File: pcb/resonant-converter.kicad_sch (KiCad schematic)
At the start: 30 parts, among them J1 Banana_Jack_Keystone_575-8, J2 Banana_Jack_Keystone_575-8, J3 Banana_Jack_Keystone_575-8, J4 Banana_Jack_Keystone_575-8, Q1 SIS472DN-T1-GE3, Q2 SIS472DN-T1-GE3, Q3 SIS472DN-T1-GE3, Q4 SIS472DN-T1-GE3, T1 B66206W1110T001, U1 UCC256610DDBR, U2 TEA2096T/1J, U4 PC817X2CSP9F, U5 TL431AIDBVR

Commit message: [#3] Add input capacitors and power indicator LED, change GND names on primary and secondary
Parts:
- added D3: LED-R-0603_KT-0603R, DW-footprints:LED_0603_1608Metric_R, symbol DW-diodes:LED-R-0603_KT-0603R
- added R10, R5: R-10k-0402, DW-footprints:R_0402_1005Metric, symbol DW-resistors:R-10k-0402
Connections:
- net GNDPWR is gone; now on net GND: C2.1, C3.1, C4.1, C5.1, C6.1, C7.1, J2.1, Q4.1 (S), Q4.2 (S), Q4.3 (S), U1.10 (GNDP)
- net GND: now also D3.1 (C); no longer D1.2 (A), D2.2 (A), Q1.1 (S), Q1.2 (S), Q1.3 (S), Q2.1 (S), Q2.2 (S), Q2.3 (S), R6.1, U2.2 (GND), U2.4 (SSB), U2.5 (SSA), U5.5 (A)
- net VCC: now also R10.2
- net at Q3.4 (G), U1.15 (HO): no longer C1.2
- net at L1.1, Q3.1 (S), Q3.2 (S)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: now also C1.2
- net GND_ISO: now reaches J4.1
- net GND_ISO: now also D1.2 (A), D2.2 (A), Q1.1 (S), Q1.2 (S), Q1.3 (S), Q2.1 (S), Q2.2 (S), Q2.3 (S), R6.1, U2.2 (GND), U2.4 (SSB), U2.5 (SSA), U5.5 (A)
- new net: D3.2 (A), R5.1
- new net: R10.1, R5.2

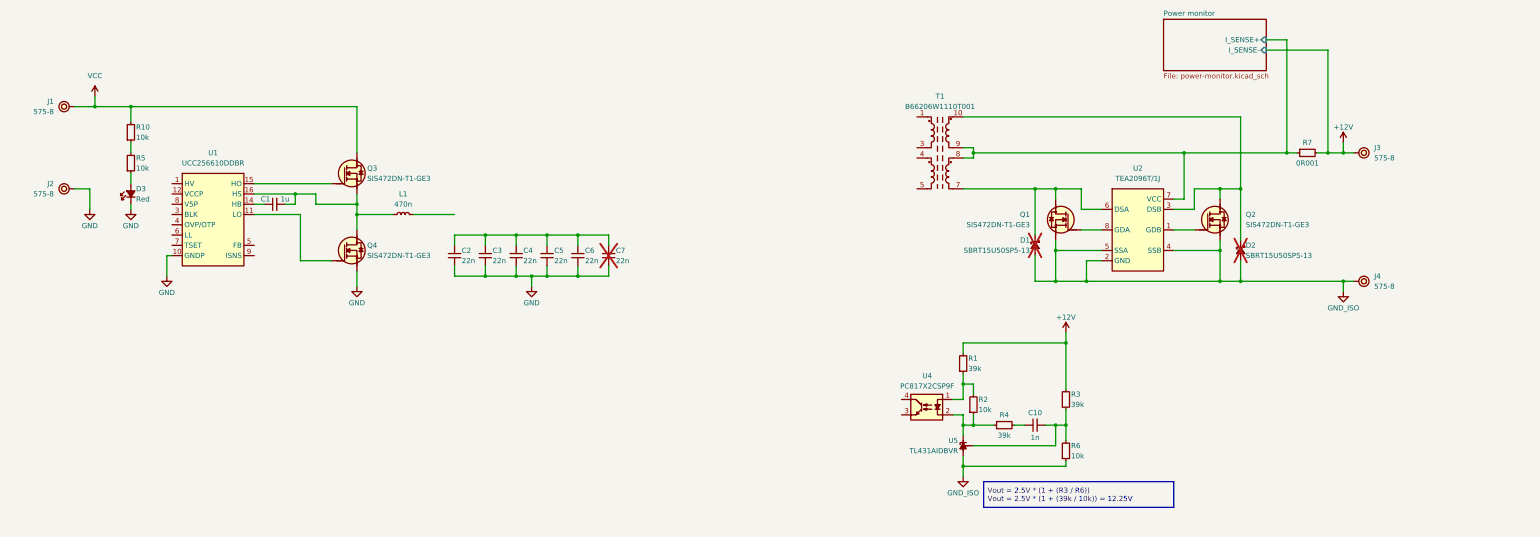
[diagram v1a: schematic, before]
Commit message: [#4] Sch: Add input and output capacitors, pri-sec interference capacitor and QWIIC connector, refactor schematic
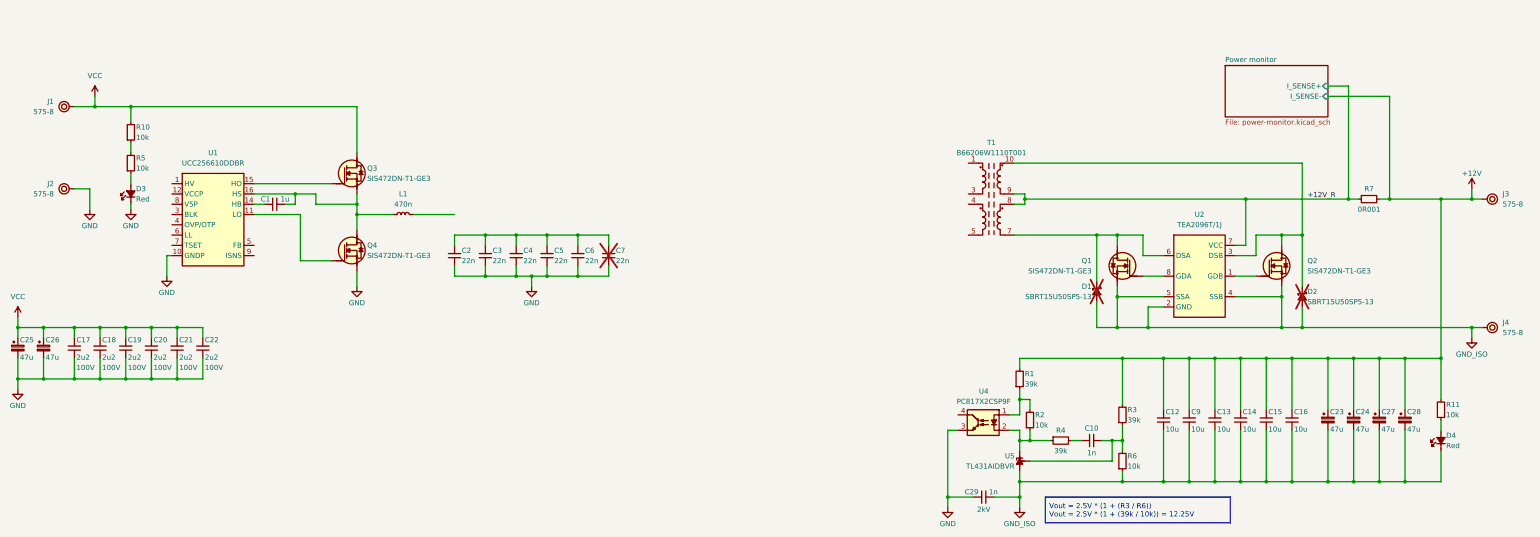
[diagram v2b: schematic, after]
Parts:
- added C12, C13, C14, C15, C16, C9: C-10u-0603, DW-footprints:C_0603_1608Metric, symbol DW-capacitors:C-10u-0603
- added C17, C18, C19, C20, C21, C22: C-2u2-100V-1206, DW-footprints:C_1206_3216Metric, symbol DW-capacitors:C-2u2-100V-1206
- added C23, C24, C25, C26, C27, C28: C_Pol_47u_100V_D8mm_H11.5, DW-footprints:C_Pol_D8mm_H11.5mm_P3.5mm, symbol DW-capacitors:C_Pol_47u_100V_D8mm_H11.5
- added C29: C-1n-2kV-1206, DW-footprints:C_1206_3216Metric, symbol DW-capacitors:C-1n-2kV-1206
- added D4: LED-R-0603_KT-0603R, DW-footprints:LED_0603_1608Metric_R, symbol DW-diodes:LED-R-0603_KT-0603R
- added R11: R-10k-0402, DW-footprints:R_0402_1005Metric, symbol DW-resistors:R-10k-0402
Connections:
- net +12V: now also C12.2, C13.2, C14.2, C15.2, C16.2, C23.1, C24.1, C27.1, C28.1, C9.2, R11.2
- net GND: now also U4.3, C17.1, C18.1, C19.1, C20.1, C21.1, C22.1, C25.2, C26.2, C29.1
- net GND_ISO: now also C12.1, C13.1, C14.1, C15.1, C16.1, C23.2, C24.2, C27.2, C28.2, C29.2, C9.1, D4.1 (C)
- net VCC: now also C17.2, C18.2, C19.2, C20.2, C21.2, C22.2, C25.1, C26.1
- net Power monitor/I_SENSE+ renamed +12V_R
- new net: D4.2 (A), R11.1
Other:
- moved on the sheet: C10, D1, D2, J3, J4, Q1, Q2, R1, R2, R3, R4, R6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

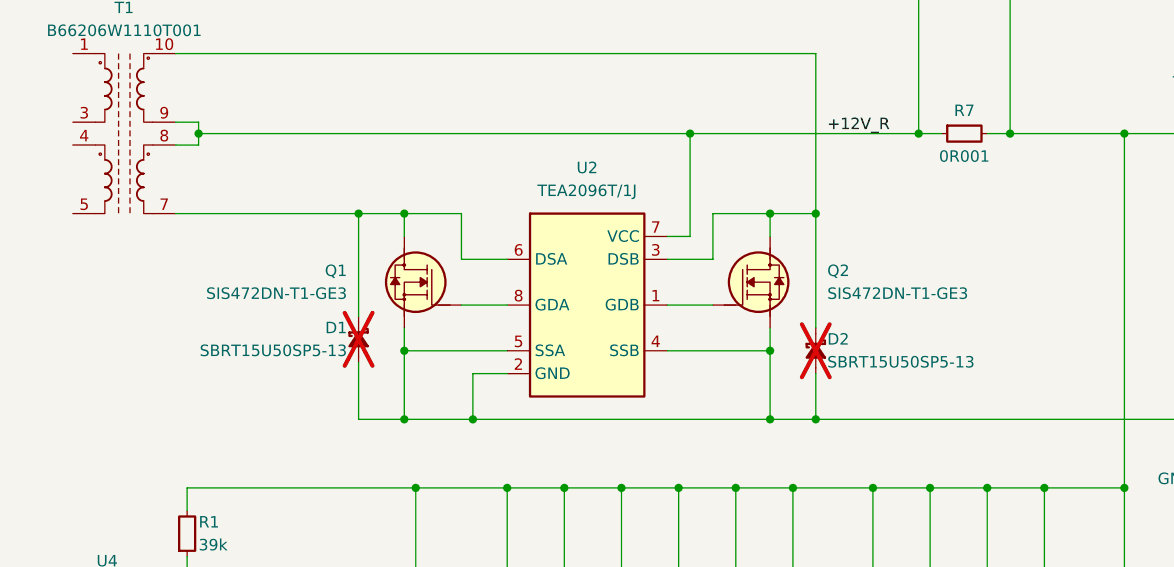
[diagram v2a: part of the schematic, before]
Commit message: [#4] Sch: Change rectifier MOSFETS
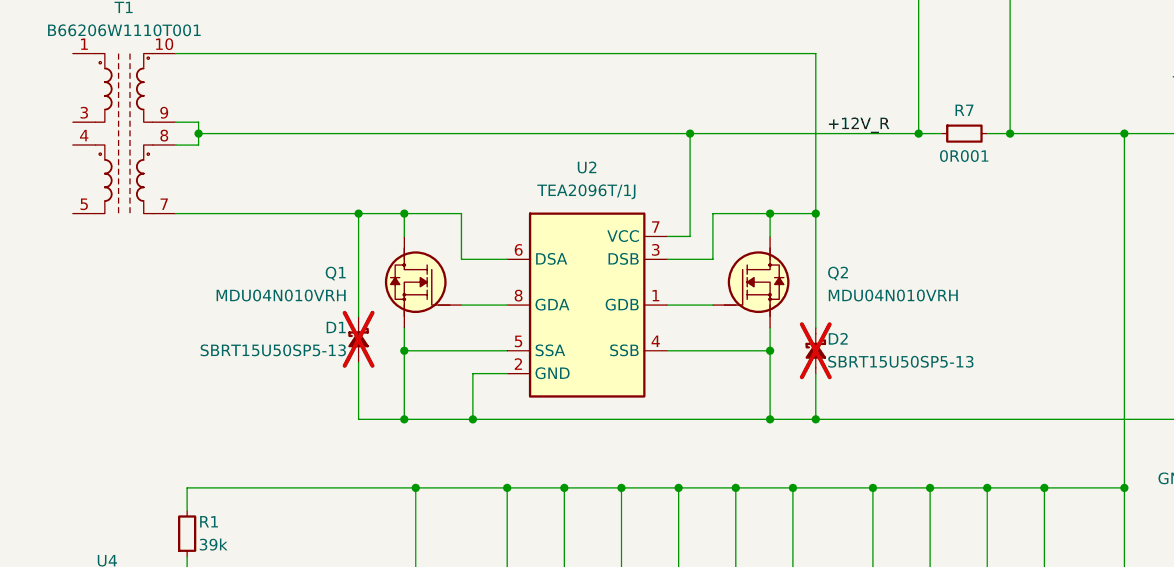
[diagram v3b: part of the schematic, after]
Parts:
- removed Q1, Q2: SIS472DN-T1-GE3, DW-footprints:PowerPAK-1212-8_Single, symbol DW-transistors:SIS472DN-T1-GE3
- added Q1, Q2: MDU04N010VRH, DW-footprints:PDFN-56-8, symbol DW-transistors:MDU04N010VRH
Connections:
- net GND_ISO: now also Q1.1 (S), Q1.2 (S), Q1.3 (S), Q2.1 (S), Q2.2 (S), Q2.3 (S)
- net at U2.1 (GDB): now also Q2.4 (G)
- net at D2.1 (C), T1.10, U2.3 (DSB): now also Q2.5 (D)
- net at D1.1 (C), T1.7, U2.6 (DSA): now also Q1.5 (D)
- net at U2.8 (GDA): now also Q1.4 (G)

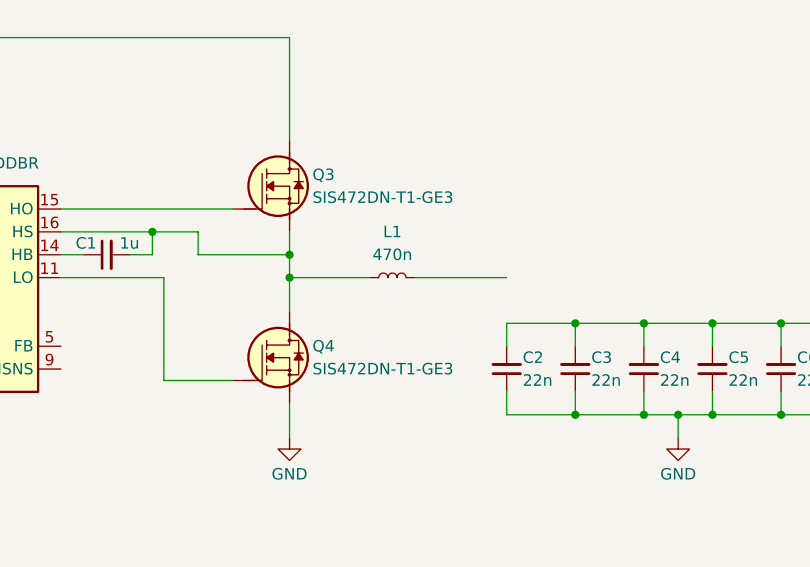
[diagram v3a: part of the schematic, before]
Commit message: [#3] Sch: Change primary side MOSFETS
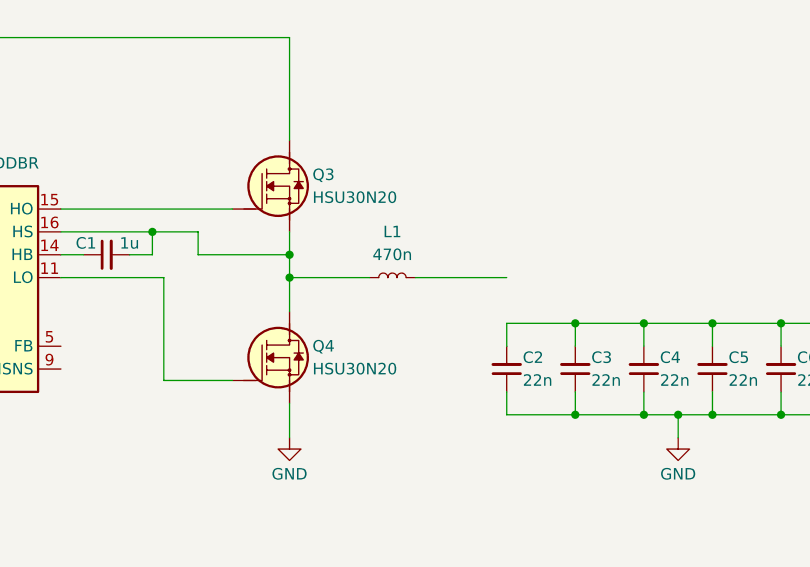
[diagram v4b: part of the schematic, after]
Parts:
- removed Q3, Q4: SIS472DN-T1-GE3, DW-footprints:PowerPAK-1212-8_Single, symbol DW-transistors:SIS472DN-T1-GE3
- added Q3, Q4: HSU30N20, DW-footprints:TO-252-3, symbol DW-transistors:HSU30N20
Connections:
- net GND: now also Q4.2 (S)
- net VCC: now also Q3.3 (D)
- net at U1.11 (LO): now also Q4.1 (G)
- net at U1.15 (HO): now also Q3.1 (G)
- net at C1.2, L1.1, U1.16 (HS): now also Q3.2 (S), Q4.3 (D)

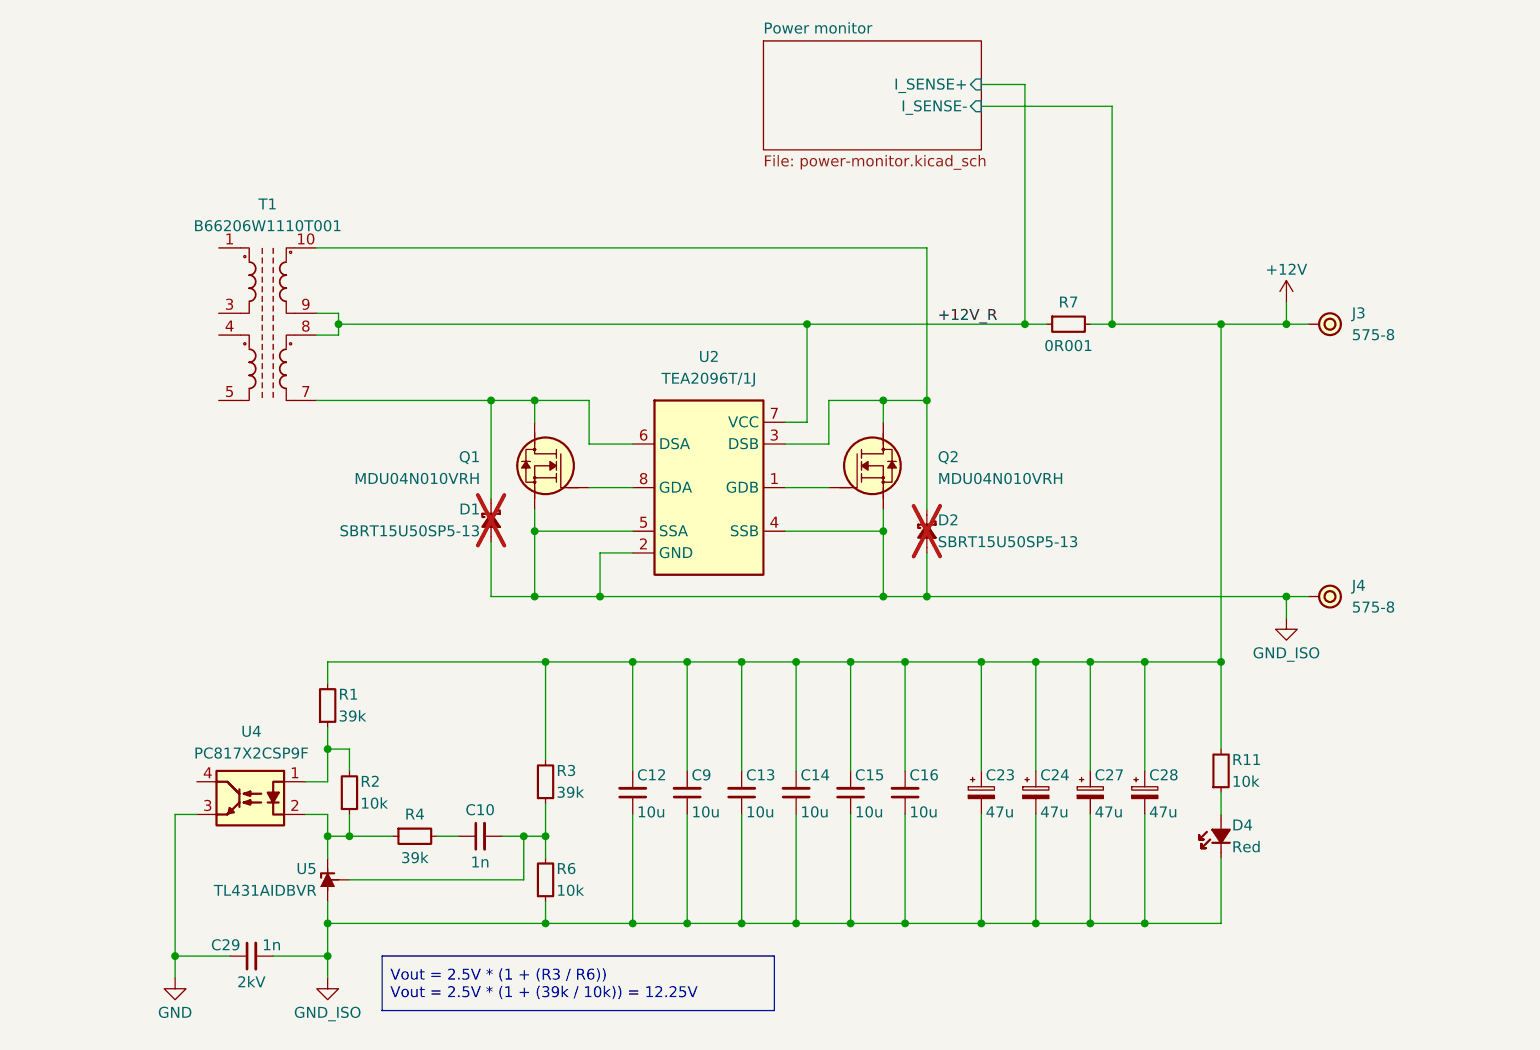
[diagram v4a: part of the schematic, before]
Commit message: [#4] Sch: Adjust feedback network component values, add optional compensation components
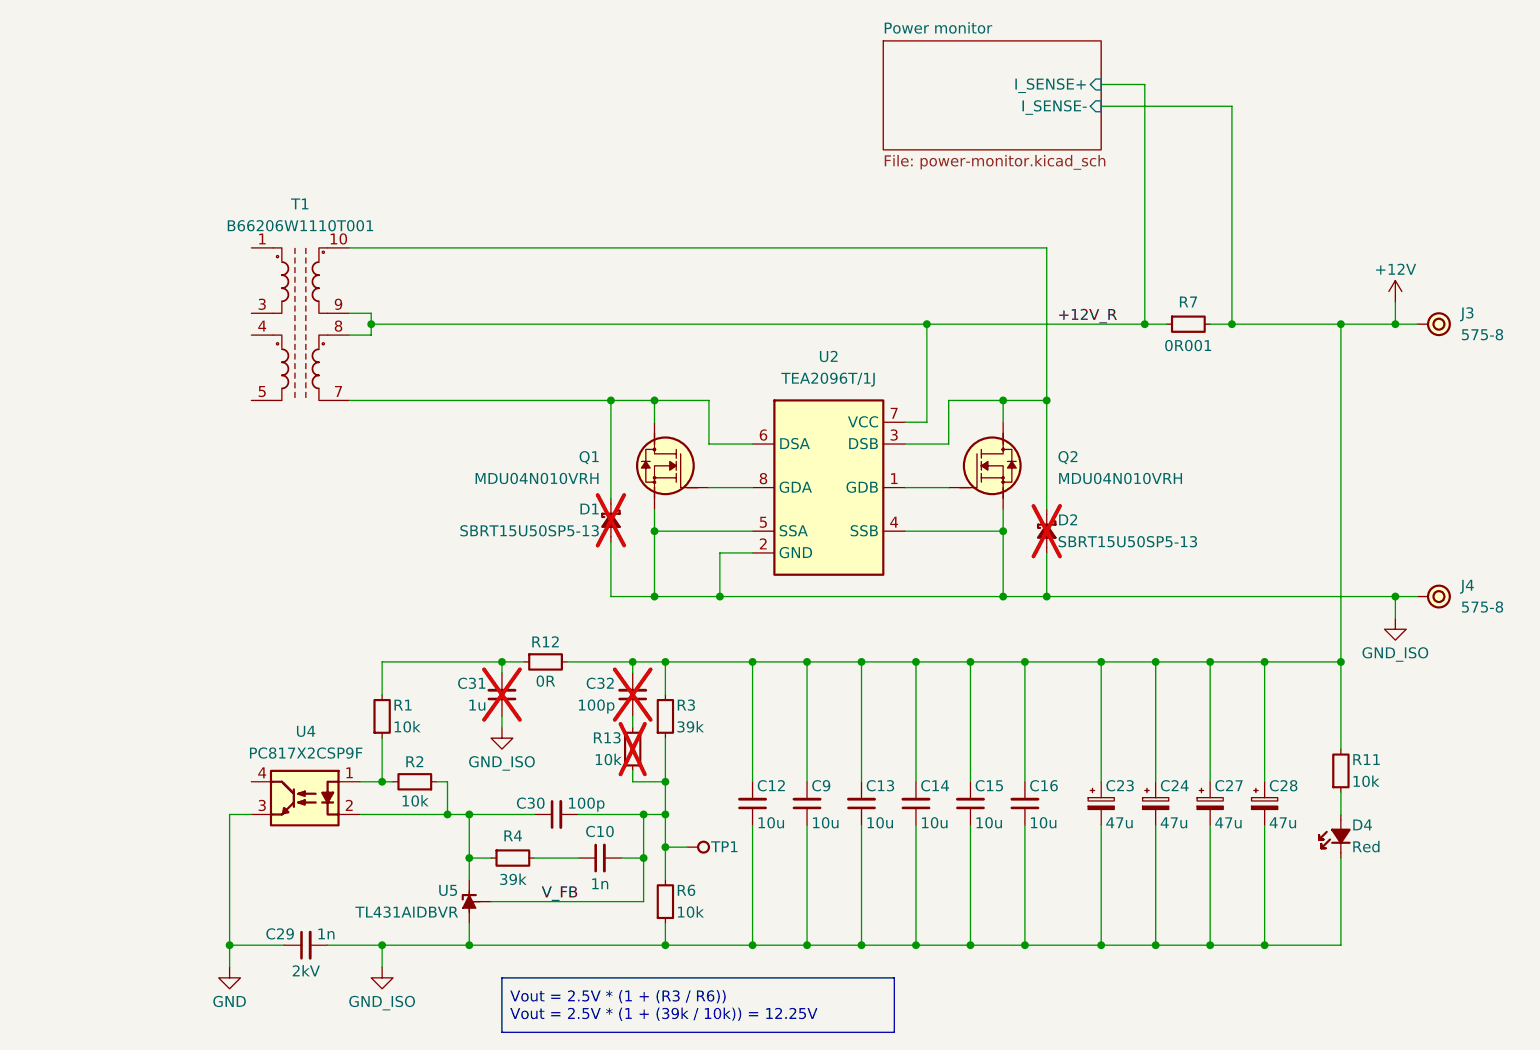
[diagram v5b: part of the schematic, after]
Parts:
- removed R1: R-39k-0402, DW-footprints:R_0402_1005Metric, symbol DW-resistors:R-39k-0402
- added C30, C32: C-100p-0402, DW-footprints:C_0402_1005Metric, symbol DW-capacitors:C-100p-0402
- added C31: C-1u-0402, DW-footprints:C_0402_1005Metric, symbol DW-capacitors:C-1u-0402
- added R1, R13: R-10k-0402, DW-footprints:R_0402_1005Metric, symbol DW-resistors:R-10k-0402
- added R12: R-0R-0402, DW-footprints:R_0402_1005Metric, symbol DW-resistors:R-0R-0402
- added TP1: TP_SMD_1mm, DW-footprints:TP_SMD_1mm, symbol DW-test-points:TP_SMD_1mm
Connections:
- net +12V: now also C32.2, R12.2
- net GND_ISO: now also C31.1
- net at R2.1, R4.1, U4.2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: now also C30.1
- net at R2.2, U4.1: now also R1.1
- net V_FB: now reaches C10.2, R3.1, R6.2, U5.4 (REF)
- net V_FB: now also C30.2, R13.1, TP1.1
- new net: C31.2, R1.2, R12.1
- new net: C32.1, R13.2
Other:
- moved on the sheet: C10, C12, C13, C14, C15, C16, C23, C24, C27, C28, C29, C9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
